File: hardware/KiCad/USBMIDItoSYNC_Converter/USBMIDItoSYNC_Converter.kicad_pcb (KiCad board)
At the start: 2 copper layers, 58 x 32 mm, 19 parts, among them J1 MJ8435, J2 MJ8435, J3 MJ8435, SW1 SW_SPDT, SW2 SW_DIP_x04, U1 MOUDLE-SEEEDUINO-XIAO, U2 TLP2368_TPL,E, U3 SN74LV1T34DBVR

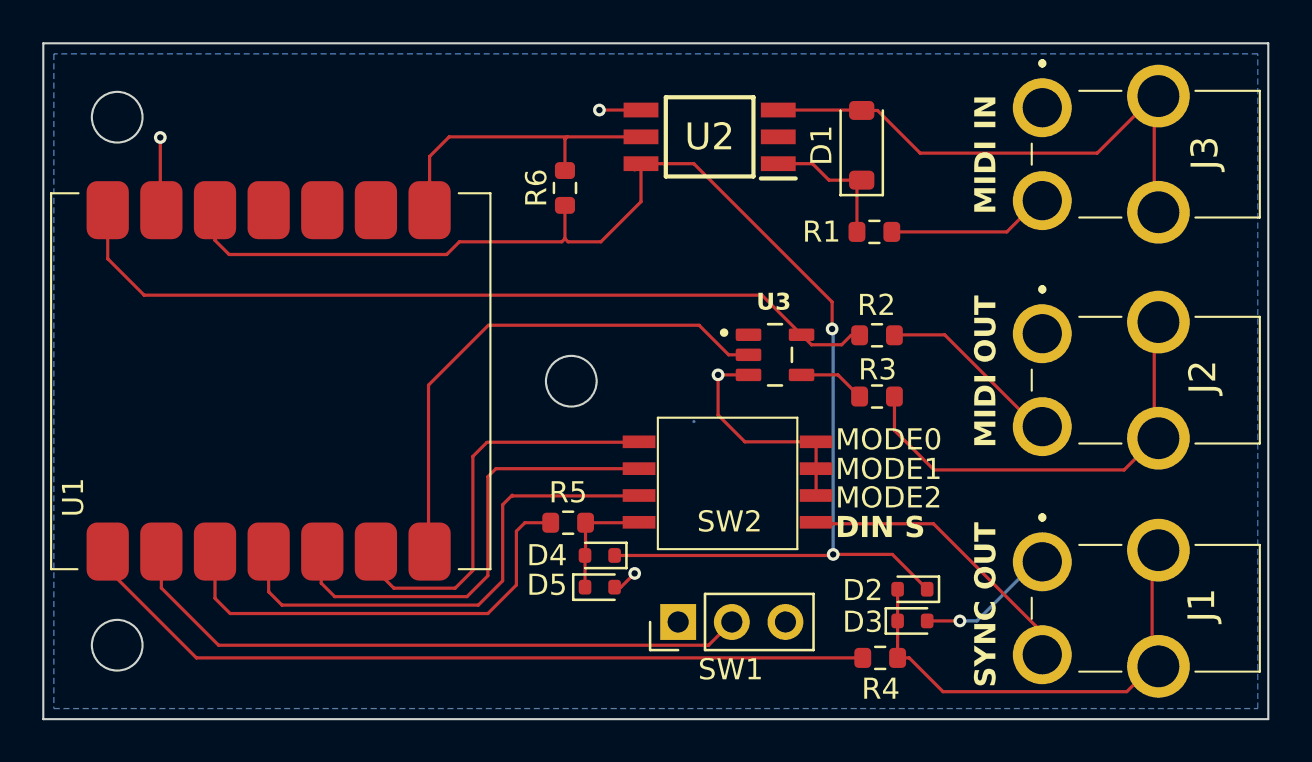
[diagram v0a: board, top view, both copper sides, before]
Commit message: fix schematic :  protection circuit
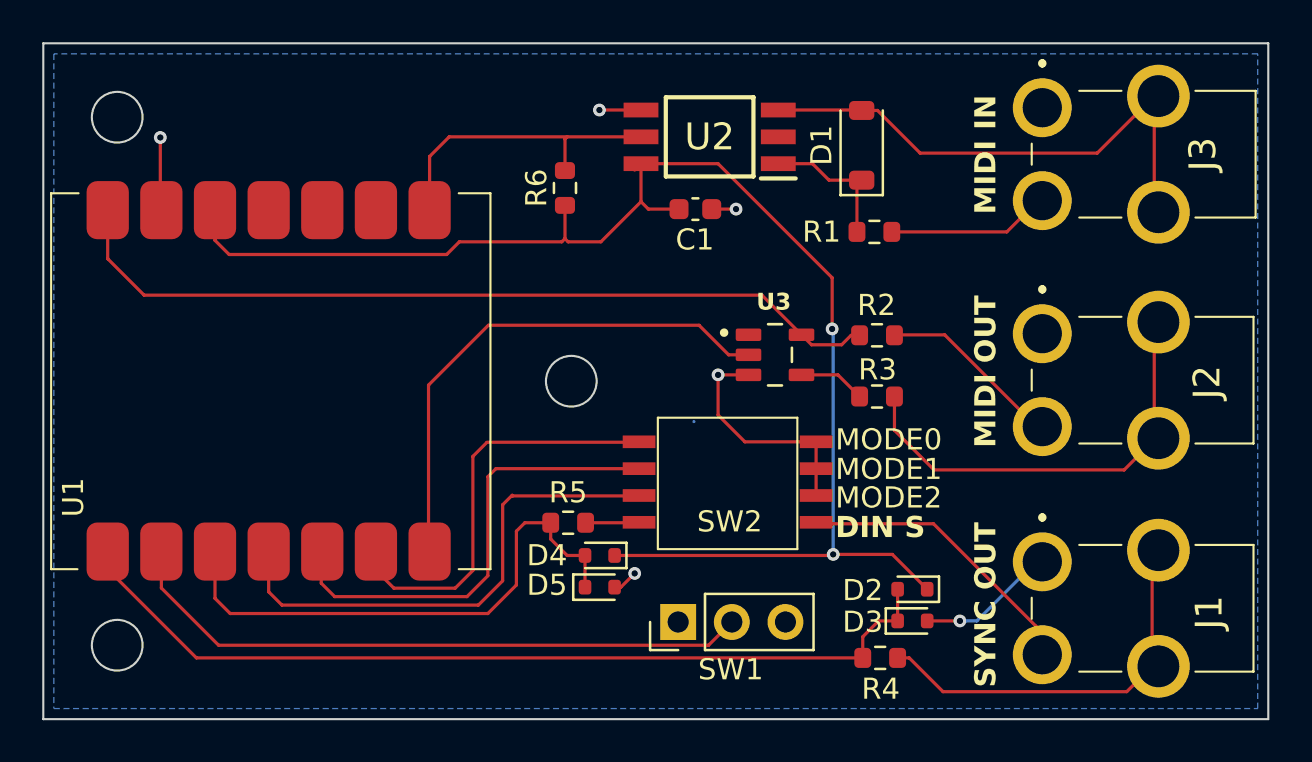
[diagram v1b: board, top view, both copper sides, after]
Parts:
- added C1: 0.1u, Capacitor_SMD:C_0603_1608Metric, F.Cu at (85.9, 90.3)
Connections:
- J1 pad 2: Net-(D2-A) -> Net-(J1-Tip)
- R4 pad 1: Net-(U1-PA02_A0_D0) -> Net-(D2-A)
- R4 pad 2: Net-(D2-A) -> Net-(J1-Tip)
- R5 pad 1: Net-(U1-PA10_A2_D2) -> Net-(D4-A)
- R5 pad 2: Net-(D4-A) -> Net-(R5-Pad2)
- SW2 pad 1: Net-(D4-A) -> Net-(R5-Pad2)
- U1 pad 1: Net-(U1-PA02_A0_D0) -> Net-(D2-A)
- U1 pad 3: Net-(U1-PA10_A2_D2) -> Net-(D4-A)
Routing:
- net Net-(U1-PA02_A0_D0): track 39.5 -> 0.00 mm
- net Net-(D2-A): track 22.0 -> 44.0 mm
- net Net-(U1-PA10_A2_D2): track 21.7 -> 0.00 mm
- net Net-(D4-A): track 5.64 -> 25.9 mm
- net Net-(J1-Tip): track 0.00 -> 18.7 mm
- net +3.3V: track 67.3 -> 69.9 mm
- net Net-(R5-Pad2): track 0.00 -> 2.58 mm
- net GND: track 24.7 -> 25.9 mm, vias 5 -> 6
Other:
- board text added: "USB MIDI to Sync Converter v1.0.1 @YuuichiAkagawa"
- board text removed: "USB MIDI to Sync Converter v1.0.0 @YuuichiAkagawa"

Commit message: fix schematic : add OSHW logo
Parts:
- added G***: LOGO, 00_MyFootprintLibs:OSHWLOGO-s-back-withtext, F.Cu at (62.6, 99.0)
